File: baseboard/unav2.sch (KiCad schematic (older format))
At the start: 12 parts, among them J2 Conn_02x24_Odd_Even, J3 IMU, J4 GPS, J5 OLED

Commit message: [UNAV2]
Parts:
- removed C1, C2, C3, C4: C, symbol agg-kicad:C
- removed D1: SCHOTTKY, symbol agg-kicad:SCHOTTKY
- removed J2: Conn_02x24_Odd_Even, symbol Connector_Generic:Conn_02x24_Odd_Even
- removed U?: STM32F407VETx, Package_QFP:LQFP-100_14x14mm_P0.5mm, symbol MCU_ST_STM32F4:STM32F407VETx
- added C? (x7): 100nF, Capacitor_SMD:C_0402_1005Metric, symbol Device:C_Small
- added C? (x2): 12p, symbol Device:C_Small
- added C? (x2): 1uF, Capacitor_SMD:C_0402_1005Metric, symbol Device:C_Small
- added C?: C, symbol agg-kicad:C
- added C?: 10n, Capacitor_SMD:C_0402_1005Metric, symbol Device:C_Small
- added C?: 10nF, Capacitor_SMD:C_0402_1005Metric, symbol Device:C_Small
- added C?: 4.7uF, Capacitor_SMD:C_0805_2012Metric, symbol Device:C_Small
- added D?: D_Schottky, symbol Device:D_Schottky
- added D?: BAT54C, symbol Device:D_Schottky_x2_KCom_AAK
- added J?: USB_B_Micro, symbol Connector:USB_B_Micro
- added JP?: BOOT, symbol Device:Jumper_NO_Small
- added L?: L_Small, symbol Device:L_Small
- added P?: SWD_TC, agg:TC2030-NL, symbol agg-kicad:SWD_TC
- added R?: 47K, Resistor_SMD:R_0402_1005Metric, symbol Device:R_Small
- added R? (x2): 22, Resistor_SMD:R_0402_1005Metric, symbol Device:R_Small
- added R?: 10K, Resistor_SMD:R_0402_1005Metric, symbol Device:R_Small
- added SW?: Reset, symbol Switch:SW_Push
- added SW?: KEY_UP, symbol Switch:SW_Push
- added SW?: KEY1, symbol Switch:SW_Push
- added SW?: KEY0, symbol Switch:SW_Push
- added U?: STM32F405RGTx, Package_QFP:LQFP-64_10x10mm_P0.5mm, symbol MCU_ST_STM32F4:STM32F405RGTx
- added Y?: 32.768K, symbol Device:Crystal
- added Y?: 8MHz, symbol Device:Resonator_Small
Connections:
- net labels added: +3.3VA, +5VDD, +5V_EXT, ADC1_IN13, ADC1_IN3, ADC_BATT_CUR, ADC_BATT_VOL, ADC_MOT1_CUR, ADC_MOT2_CUR, ADC_TEMP, BOOT0, GNDA, I2C1_SCL, I2C1_SDA, I_FAN_INDEX, I_KEY0, I_KEY1, I_KEY_UP, NRST, O_LED1, O_LED2, O_MOT_ENABLE, O_PWR_MAIN_EN, O_PWR_SBC_EN, PA0, PA1, PA10, PA11, PA12, PA13, PA14, PA2, PA3, PA5, PA6, PA7, PA9, PB0, PB4_SPI1_MISO, PC0, PC1, PC13, PC2, PC3, PC4, PC5, PC6, PC7, PD2, SWCK, SWDIO, TIM_AUX3_PWM, TIM_ENC1_A, TIM_ENC1_B, TIM_ENC3_A, TIM_FAN_PWM, TIM_MOT1_A, TIM_MOT1_B, TIM_MOT2_A, TIM_MOT2_B, USART1_RX, USART1_TX, USART2_RX, USART2_TX, USB_OTG_FS_DM, USB_OTG_FS_DP, VBATT, VDDA
- net labels removed: BT0, PA0_KEY_UP, PA10_USART1_RX, PA11_USB_OTG_FS_DM, PA12_USB_OTG_FS_DP, PA1_ENC3_B, PA2_ADC_TEMP, PA3_ADC1_IN3, PA5_TIM_ENC3_A, PA6_O_LED1, PA7_O_LED2, PA9_USART1_TX, PB0_O_FLASH_CS, PC0_ADC_MOT1_CUR, PC10_SDIO_D2, PC11_SDIO_D3, PC12_SDIO_CK, PC13_I_FAN_INDEX, PC1_ADC_MOT2_CUR, PC2_ADC_MOT3_CUR, PC3_ADC1_IN13, PC4_ADC_BATT_CUR, PC5_ADC_BATT_VOL, PC6_TIM_ENC1_A, PC7_TIM_ENC1_B, PC8_SDIO_D0, PC9_SDIO_D1, PD2__SDIO_CMD, PE12_TIM_MOT3_A, PE13_TIM_MOT3_A
- wire segments 172 -> 234
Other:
- note removed: "PB4/SPI1_MISO is \nmissing from header!!!"
- moved on the sheet: C5, C6, J3, J4, J5

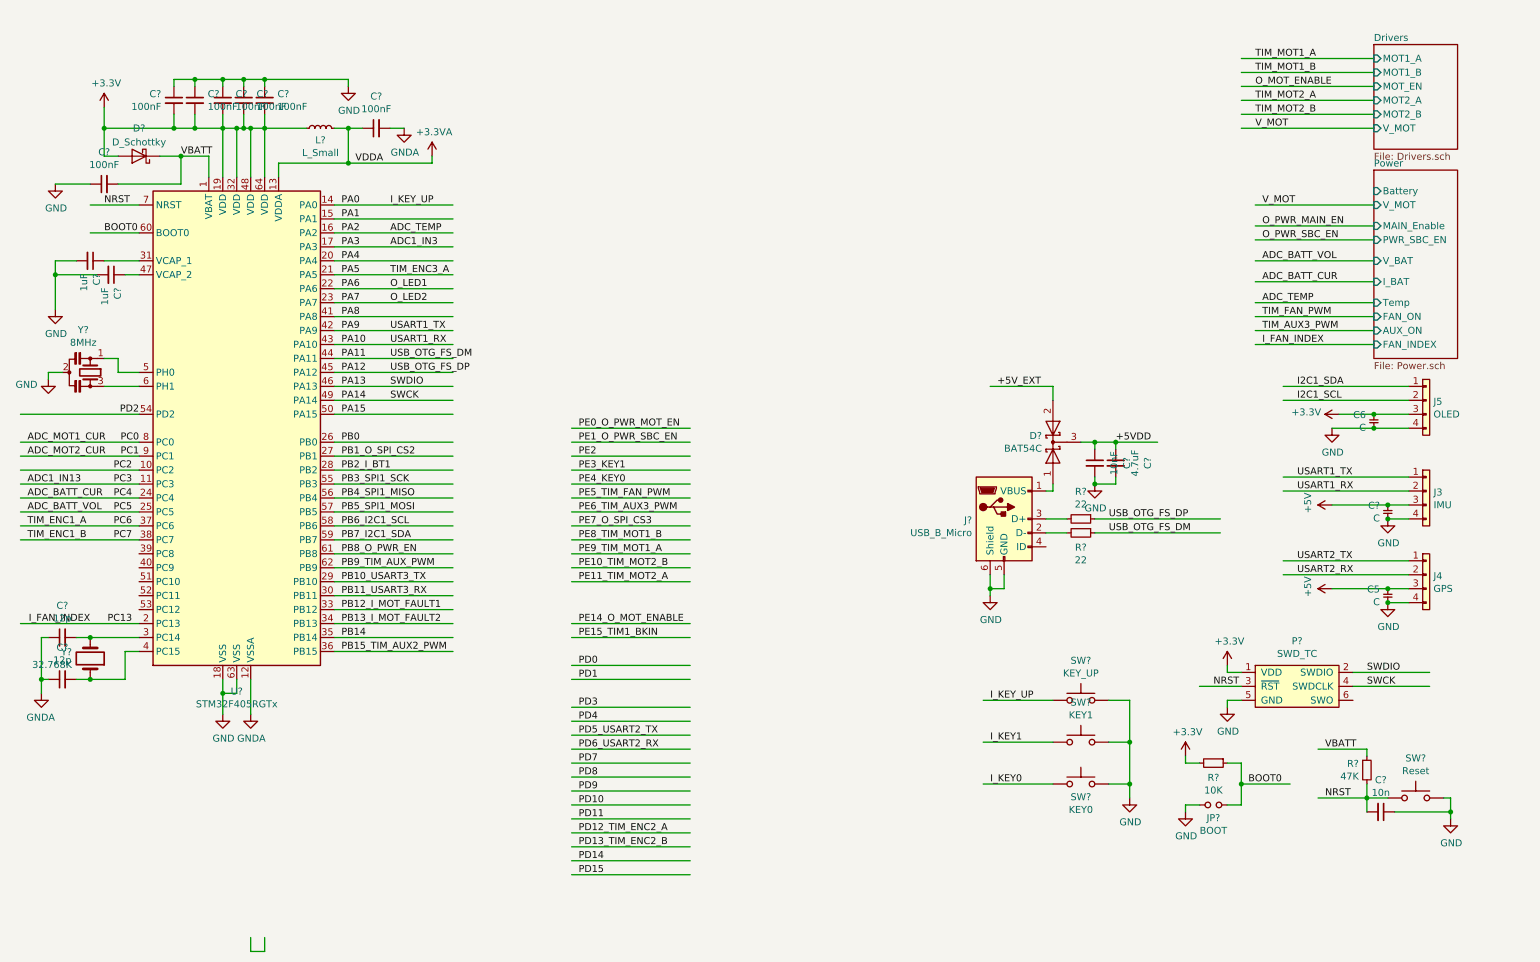
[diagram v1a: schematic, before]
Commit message: standalone version of unav2 based on stm32f405rgt
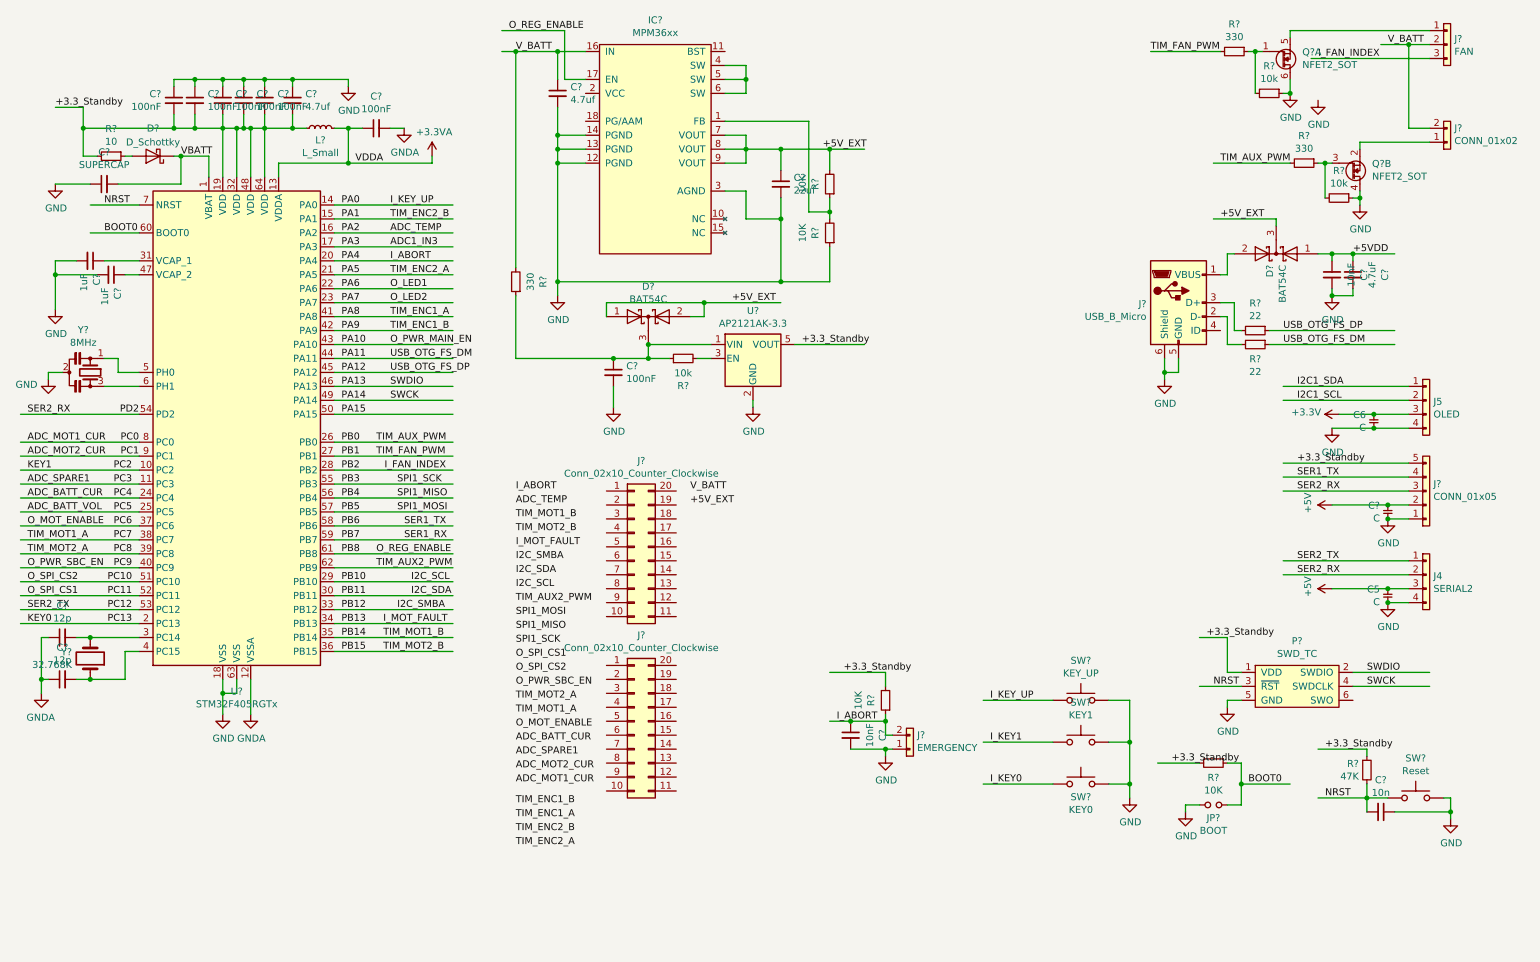
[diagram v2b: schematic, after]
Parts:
- removed J3: IMU, symbol agg-kicad:CONN_01x04
- added C? (x2): 4.7uf, Capacitor_SMD:C_0805_2012Metric, symbol Device:C_Small
- added C?: 22uf, Capacitor_SMD:C_0805_2012Metric, symbol Device:C_Small
- added C?: 100nF, Capacitor_SMD:C_0402_1005Metric, symbol Device:C_Small
- added C?: 10nF, Capacitor_SMD:C_0402_1005Metric, symbol Device:C_Small
- added D?: BAT54C, symbol Device:D_Schottky_x2_KCom_AAK
- added IC?: MPM36xx, agg:QFN-20-MPS-3x5x1.6mm, symbol agg-kicad:MPM36xx
- added J?: CONN_01x05, symbol agg-kicad:CONN_01x05
- added J?: EMERGENCY, symbol agg-kicad:CONN_01x02
- added J?: FAN, symbol agg-kicad:CONN_01x03
- added J?: CONN_01x02, symbol agg-kicad:CONN_01x02
- added J? (x2): Conn_02x10_Counter_Clockwise, symbol Connector_Generic:Conn_02x10_Counter_Clockwise
- added Q? (x2): NFET2_SOT, symbol agg-kicad:NFET2_SOT
- added R?: 10, Resistor_SMD:R_0402_1005Metric, symbol Device:R_Small
- added R? (x3): 10K, Resistor_SMD:R_0402_1005Metric, symbol Device:R_Small
- added R? (x3): 330, Resistor_SMD:R_0402_1005Metric, symbol Device:R_Small
- added R? (x3): 10k, Resistor_SMD:R_0402_1005Metric, symbol Device:R_Small
- added U?: AP2121AK-3.3, Package_TO_SOT_SMD:SOT-23-5, symbol Regulator_Linear:AP2112K-3.3
- C?: value 100nF -> SUPERCAP; footprint Capacitor_SMD:C_0402_1005Metric -> Capacitor_SMD:C_Elec_10x10.2
- J4: value GPS -> SERIAL2
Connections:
- net labels added: +3.3_Standby, ADC_SPARE1, I2C_SCL, I2C_SDA, I2C_SMBA, I_ABORT, I_MOT_FAULT, KEY0, KEY1, O_REG_ENABLE, O_SPI_CS1, O_SPI_CS2, PB1, PB10, PB11, PB12, PB13, PB15, PB2, PB3, PB4, PB5, PB6, PB7, PB8, PC10, PC11, PC12, PC8, PC9, SER1_RX, SER1_TX, SER2_RX, SER2_TX, SPI1_MISO, SPI1_MOSI, SPI1_SCK, TIM_AUX2_PWM, TIM_AUX_PWM, TIM_ENC2_A, TIM_ENC2_B, V_BATT
- net labels removed: ADC1_IN13, PB10_USART3_TX, PB11_USART3_RX, PB12_I_MOT_FAULT1, PB13_I_MOT_FAULT2, PB15_TIM_AUX2_PWM, PB1_O_SPI_CS2, PB2_I_BT1, PB3_SPI1_SCK, PB4_SPI1_MISO, PB5_SPI1_MOSI, PB6_I2C1_SCL, PB7_I2C1_SDA, PB8_O_PWR_EN, PB9_TIM_AUX_PWM, PD0, PD1, PD10, PD11, PD12_TIM_ENC2_A, PD13_TIM_ENC2_B, PD14, PD15, PD3, PD4, PD5_USART2_TX, PD6_USART2_RX, PD7, PD8, PD9, PE0_O_PWR_MOT_EN, PE10_TIM_MOT2_B, PE11_TIM_MOT2_A, PE14_O_MOT_ENABLE, PE15_TIM1_BKIN, PE1_O_PWR_SBC_EN, PE2, PE3_KEY1, PE4_KEY0, PE5_TIM_FAN_PWM, PE6_TIM_AUX3_PWM, PE7_O_SPI_CS3, PE8_TIM_MOT1_B, PE9_TIM_MOT1_A, TIM_AUX3_PWM, TIM_ENC3_A, USART1_RX, USART1_TX, USART2_RX, USART2_TX, V_MOT
- wire segments 234 -> 295
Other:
- moved on the sheet: C?, D?, J?, R?

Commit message: updates
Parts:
- SW1, SW2, SW3, SW4: renamed from SW?; footprint (none) -> Button_Switch_SMD:SW_SPST_B3U-1000P
- gave numbers to parts that had none: 53
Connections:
- wire segments 295 -> 337
